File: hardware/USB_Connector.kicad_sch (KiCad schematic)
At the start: 30 parts, among them J1 USB_C_Receptacle, J13 Conn_01x04_Male, J2 USB_B_Micro, Q1 Q_Dual_NMOS_G1S2G2D2S1D1, U11 TPS2121, U5 USB3346, X1 SiT1602B

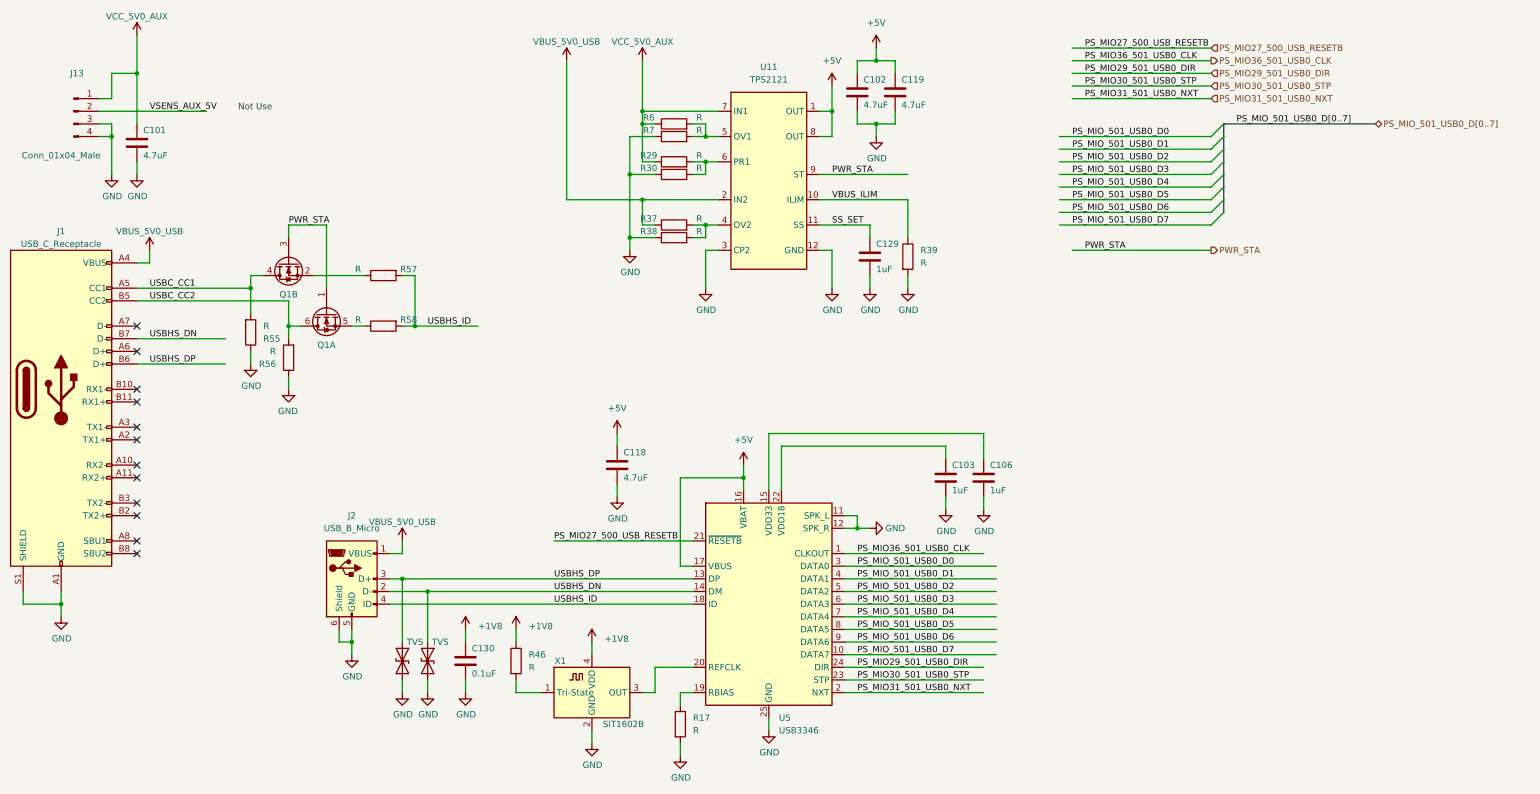
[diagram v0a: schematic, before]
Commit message: add sdio level shift ciruit
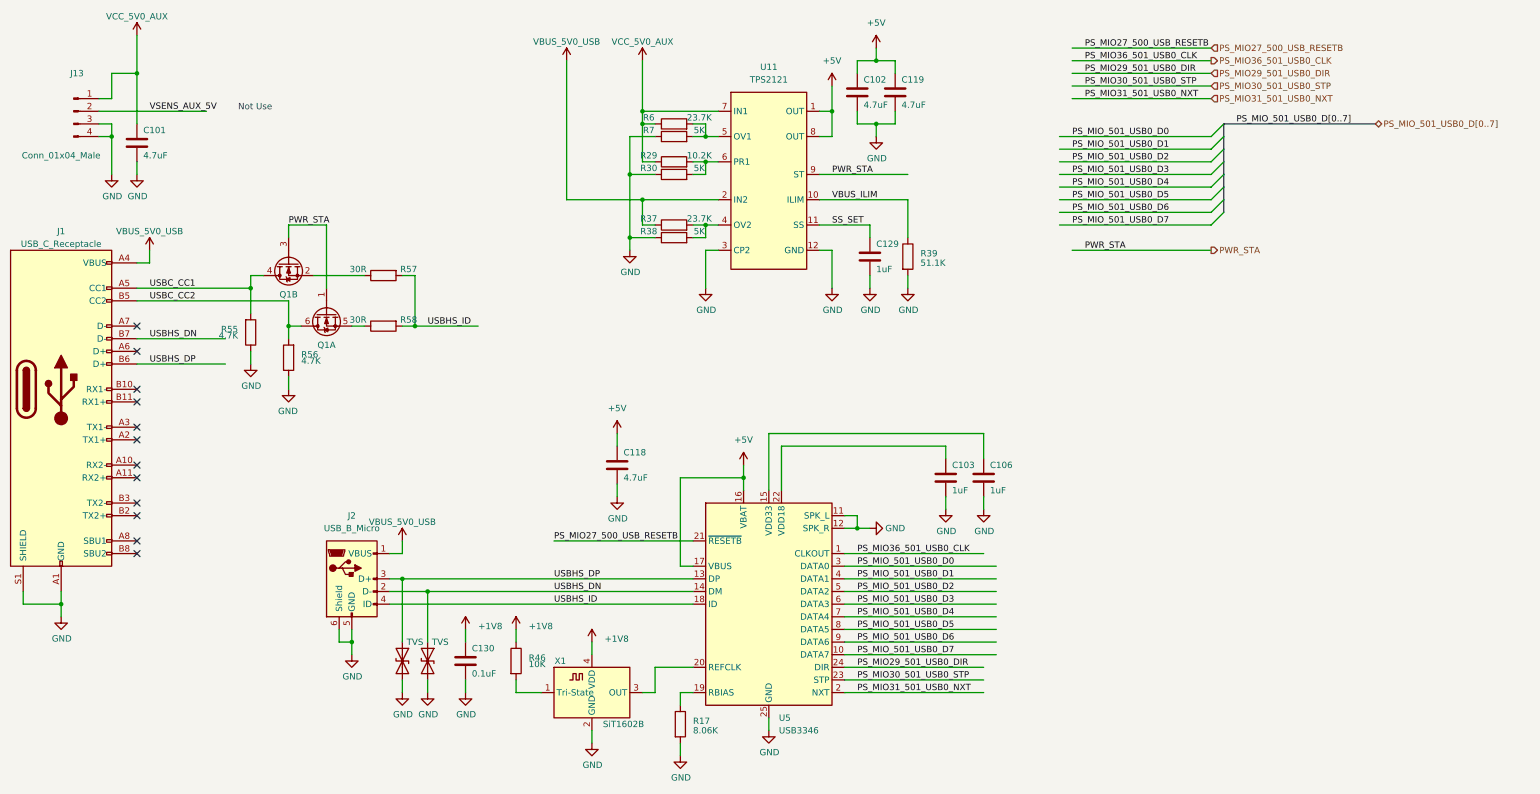
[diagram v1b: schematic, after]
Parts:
- Q1: value Q_Dual_NMOS_G1S2G2D2S1D1 -> Q_Dual_NMOS_PMDXB600UNE
- R17: value R -> 8.06K
- R29: value R -> 10.2K
- R30, R38, R7: value R -> 5K
- R37, R6: value R -> 23.7K
- R39: value R -> 51.1K
- R46: value R -> 10K
- R55, R56: value R -> 4.7K
- R57, R58: value R -> 30R
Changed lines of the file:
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@@
-(kicad_sch (version 20220104) (generator eeschema)
+(kicad_sch (version 20220126) (generator eeschema)
   (paper "A3")
   (junction (at 157.48 129.54) (diameter 0) (color 0 0 0 0)
@@
   )
   (symbol (lib_id "Device:R") (at 281.94 115.57 0) (unit 1)
-    (in_bom yes) (on_board yes) (fields_autoplaced)
-    (property "Reference" "R39" (id 0) (at 284.48 114.2999 0)
-      (effects (font (size 1.27 1.27)) (justify left))
-    )
-    (property "Value" "R" (id 1) (at 284.48 116.8399 0)
+    (in_bom yes) (on_board yes)
+    (property "Reference" "R39" (id 0) (at 284.48 114.935 0)
+      (effects (font (size 1.27 1.27)) (justify left))
+    )
+    (property "Value" "51.1K" (id 1) (at 284.48 116.84 0)
       (effects (font (size 1.27 1.27)) (justify left))
     )
@@
   (symbol (lib_id "Device:R") (at 149.86 130.81 0) (mirror x) (unit 1)
     (in_bom yes) (on_board yes) (fields_autoplaced)
-    (property "Reference" "R55" (id 0) (at 152.4 132.0801 0)
-      (effects (font (size 1.27 1.27)) (justify left))
-    )
-    (property "Value" "R" (id 1) (at 152.4 129.5401 0)
-      (effects (font (size 1.27 1.27)) (justify left))
+    (property "Reference" "R55" (id 0) (at 147.32 130.175 0)
+      (effects (font (size 1.27 1.27)) (justify right))
+    )
+    (property "Value" "4.7K" (id 1) (at 147.32 131.445 0)
+      (effects (font (size 1.27 1.27)) (justify right))
     )
     (property "Footprint" "Resistor_SMD:R_0201_0603Metric" (id 2) (at 148.082 130.81 90)
@@
       (effects (font (size 1.27 1.27)))
     )
-    (property "Value" "R" (id 1) (at 240.03 90.17 90)
+    (property "Value" "5K" (id 1) (at 240.03 90.17 90)
       (effects (font (size 1.27 1.27)))
     )
@@
       (effects (font (size 1.27 1.27)))
     )
-    (property "Value" "R" (id 1) (at 240.03 110.49 90)
+    (property "Value" "5K" (id 1) (at 240.03 110.49 90)
       (effects (font (size 1.27 1.27)))
     )
@@
       (effects (font (size 1.27 1.27)))
     )
-    (property "Value" "R" (id 1) (at 171.45 128.27 90)
+    (property "Value" "30R" (id 1) (at 171.45 128.27 90)
       (effects (font (size 1.27 1.27)))
     )
@@
       (effects (font (size 1.27 1.27)))
     )
-    (property "Value" "Q_Dual_NMOS_G1S2G2D2S1D1" (id 1) (at 165.735 133.35 0)
+    (property "Value" "Q_Dual_NMOS_PMDXB600UNE" (id 1) (at 165.735 133.35 0)
       (effects (font (size 1.27 1.27)) (justify left) hide)
     )
@@
       (effects (font (size 1.27 1.27)))
     )
-    (property "Value" "R" (id 1) (at 240.03 97.79 90)
+    (property "Value" "5K" (id 1) (at 240.03 97.79 90)
       (effects (font (size 1.27 1.27)))
     )
@@
       (effects (font (size 1.27 1.27)))
     )
-    (property "Value" "R" (id 1) (at 240.03 107.95 90)
+    (property "Value" "23.7K" (id 1) (at 240.03 107.95 90)
       (effects (font (size 1.27 1.27)))
     )
@@
       (effects (font (size 1.27 1.27)))
     )
-    (property "Value" "R" (id 1) (at 240.03 95.25 90)
+    (property "Value" "10.2K" (id 1) (at 240.03 95.25 90)
       (effects (font (size 1.27 1.27)))
     )
@@
   (symbol (lib_id "Device:R") (at 157.48 135.89 180) (unit 1)
     (in_bom yes) (on_board yes) (fields_autoplaced)
-    (property "Reference" "R56" (id 0) (at 154.94 137.1601 0)
-      (effects (font (size 1.27 1.27)) (justify left))
-    )
-    (property "Value" "R" (id 1) (at 154.94 134.6201 0)
-      (effects (font (size 1.27 1.27)) (justify left))
+    (property "Reference" "R56" (id 0) (at 160.02 135.255 0)
+      (effects (font (size 1.27 1.27)) (justify right))
+    )
+    (property "Value" "4.7K" (id 1) (at 160.02 136.525 0)
+      (effects (font (size 1.27 1.27)) (justify right))
     )
     (property "Footprint" "Resistor_SMD:R_0201_0603Metric" (id 2) (at 159.258 135.89 90)
@@
       (effects (font (size 1.27 1.27)))
     )
-    (property "Value" "R" (id 1) (at 240.03 87.63 90)
+    (property "Value" "23.7K" (id 1) (at 240.03 87.63 90)
       (effects (font (size 1.27 1.27)))
     )
@@
   (symbol (lib_id "Device:R") (at 203.2 196.85 0) (unit 1)
     (in_bom yes) (on_board yes) (fields_autoplaced)
-    (property "Reference" "R46" (id 0) (at 205.74 195.5799 0)
-      (effects (font (size 1.27 1.27)) (justify left))
-    )
-    (property "Value" "R" (id 1) (at 205.74 198.1199 0)
+    (property "Reference" "R46" (id 0) (at 205.74 196.215 0)
+      (effects (font (size 1.27 1.27)) (justify left))
+    )
+    (property "Value" "10K" (id 1) (at 205.74 197.485 0)
       (effects (font (size 1.27 1.27)) (justify left))
     )
@@
   )
   (symbol (lib_id "Device:R") (at 236.22 209.55 0) (unit 1)
-    (in_bom yes) (on_board yes) (fields_autoplaced)
-    (property "Reference" "R17" (id 0) (at 238.76 208.2799 0)
-      (effects (font (size 1.27 1.27)) (justify left))
-    )
-    (property "Value" "R" (id 1) (at 238.76 210.8199 0)
+    (in_bom yes) (on_board yes)
+    (property "Reference" "R17" (id 0) (at 238.76 208.915 0)
+      (effects (font (size 1.27 1.27)) (justify left))
+    )
+    (property "Value" "8.06K" (id 1) (at 238.76 210.82 0)
       (effects (font (size 1.27 1.27)) (justify left))
     )
@@
       (effects (font (size 1.27 1.27)))
     )
-    (property "Value" "R" (id 1) (at 171.45 118.11 90)
+    (property "Value" "30R" (id 1) (at 171.45 118.11 90)
       (effects (font (size 1.27 1.27)))
     )
@@
       (effects (font (size 1.27 1.27)))
     )
-    (property "Value" "Q_Dual_NMOS_G1S2G2D2S1D1" (id 1) (at 158.115 123.19 0)
+    (property "Value" "Q_Dual_NMOS_PMDXB600UNE" (id 1) (at 158.115 123.19 0)
       (effects (font (size 1.27 1.27)) (justify left) hide)
     )

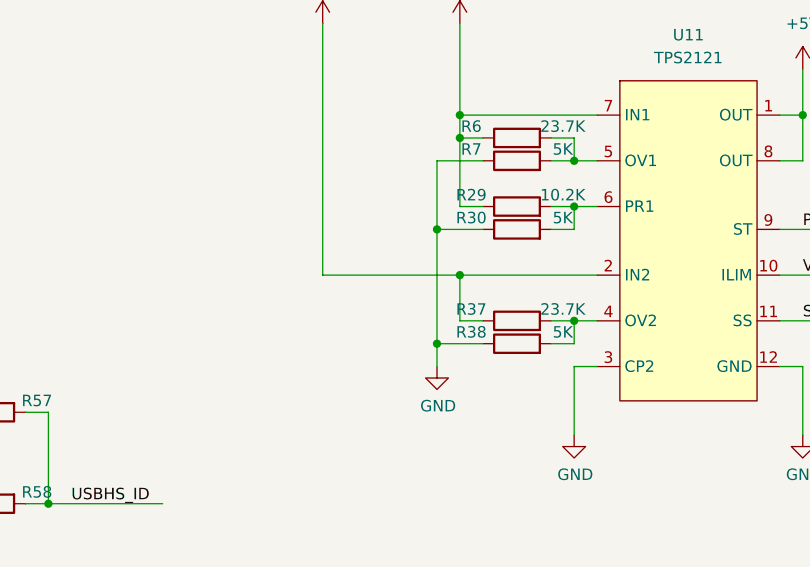
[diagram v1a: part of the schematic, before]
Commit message: Modify wrong DCDC TPS62088 package Panelize PCB Add manufacture requirements files
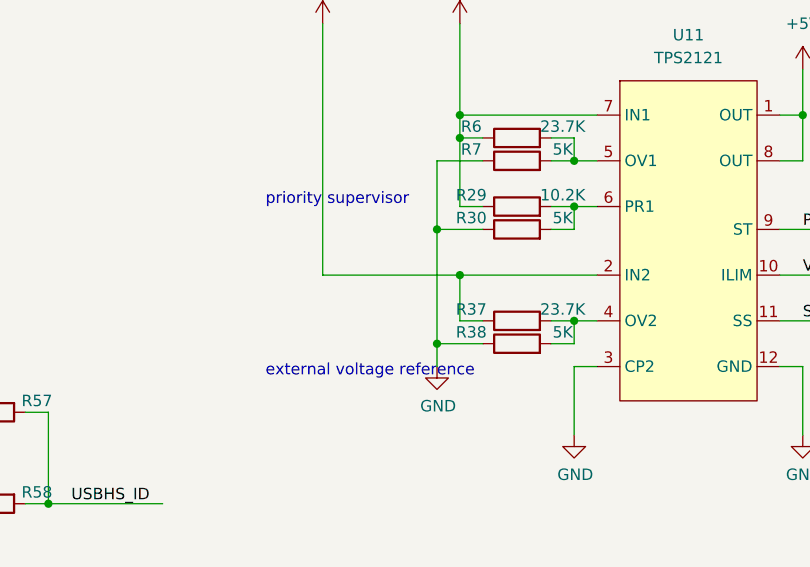
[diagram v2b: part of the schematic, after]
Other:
- note added: "external voltage reference"
- note added: "priority supervisor"
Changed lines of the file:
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@@
     (stroke (width 0) (type default))
+  )
+  (text "external voltage reference" (at 207.01 115.57 0)
+    (effects (font (size 1.27 1.27)) (justify left bottom))
   )
   (text "Not Use" (at 147.32 86.36 0)
     (effects (font (size 1.27 1.27)) (justify left bottom))
   )
+  (text "priority supervisor" (at 207.01 96.52 0)
+    (effects (font (size 1.27 1.27)) (justify left bottom))
+  )
